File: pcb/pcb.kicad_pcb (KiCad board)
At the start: 2 copper layers, 35 x 88 mm, 41 parts, among them J1 NMJ4HCD2, J2 NMJ4HCD2, J3 694106301002, SW1 FSWITCH, U1 RC4558, U2 L78L09

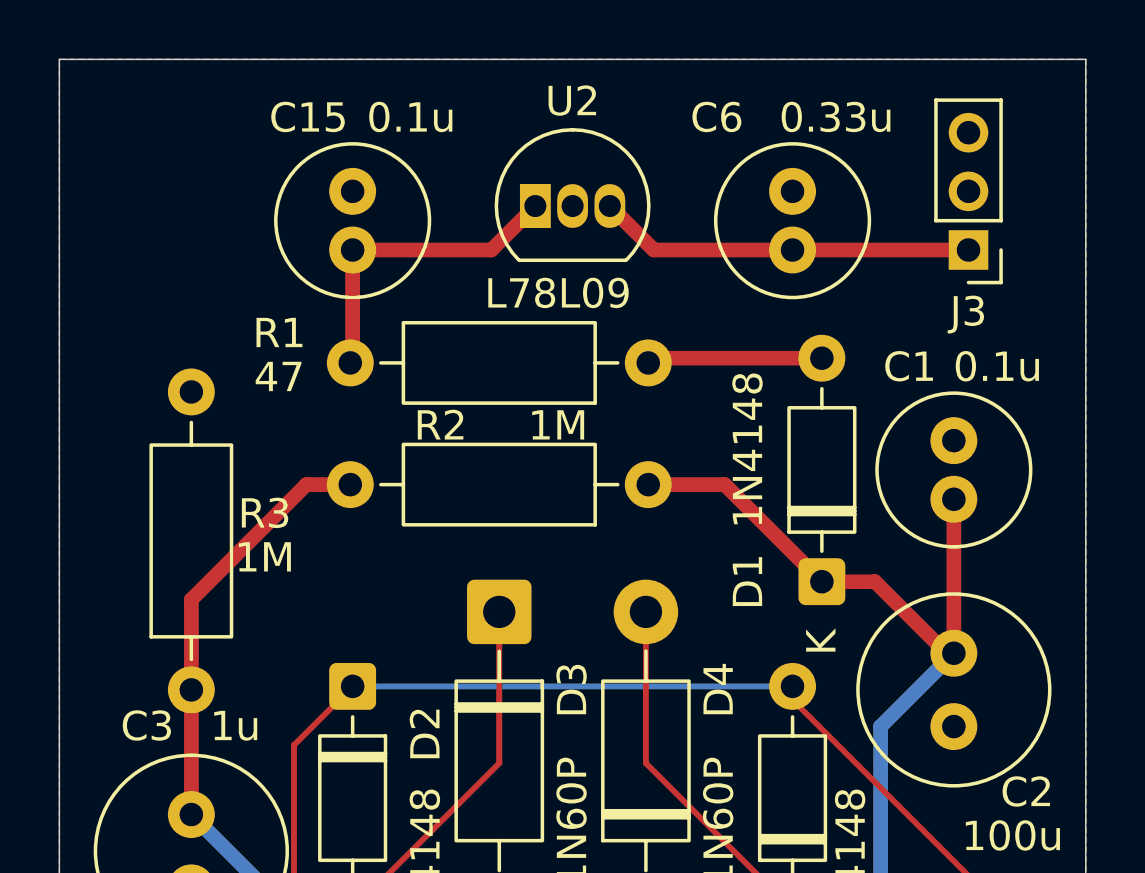
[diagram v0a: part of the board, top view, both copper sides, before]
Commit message: Fix reverse polarity protection diode - Move ahead of regulator
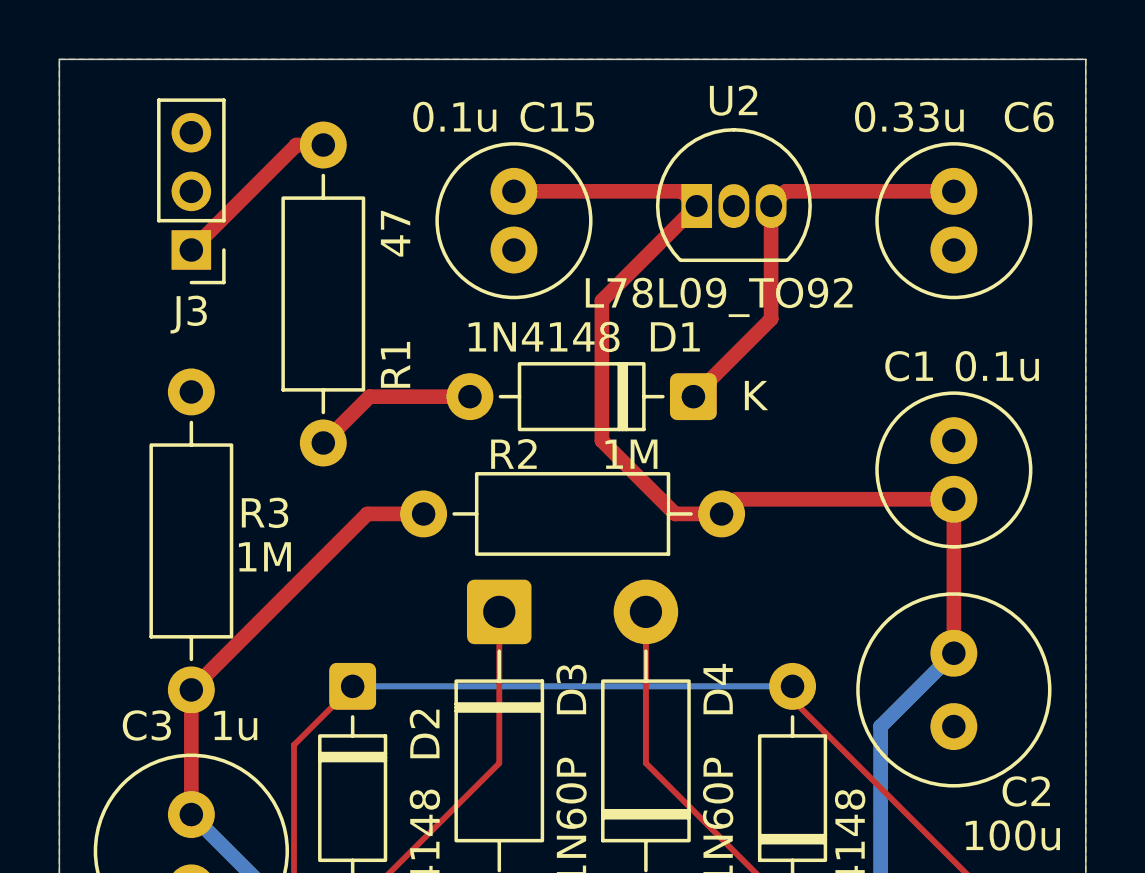
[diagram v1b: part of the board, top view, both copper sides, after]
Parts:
- U2: value L78L09 -> L78L09_TO92
- moved J3 26.5 mm to (162.0, 68.5)
- moved R1 11.4 mm to (166.5, 75.1), turned to 90 degrees
- moved D1 7.68 mm to (179.1, 73.5), turned to 180 degrees
- moved C15 5.85 mm to (173.0, 66.5), turned to -90 degrees
- moved C6 5.85 mm to (188.0, 66.5), turned to -90 degrees
- moved U2 5.50 mm to (179.2, 67.0)
- moved R2 2.69 mm to (180.1, 77.5)
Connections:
- C1 pad 1: /VCC -> /V9
- C14 pad 2: /VCC -> /V9
- C2 pad 1: /VCC -> /V9
- C6 pad 1: /VCCRAW -> Net-(D1-K)
- D1 pad 1: /VCC -> Net-(D1-K)
- R1 pad 2: /V9 -> /VCCRAW
- R2 pad 1: /VCC -> /V9
- SW1 pad 4: /VCC -> /V9
- U1 pad 8: /VCC -> /V9
- U2 pad 3: /VCCRAW -> Net-(D1-K)
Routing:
- net /V9: track 10.7 -> 97.1 mm
- net /VCC: track 80.9 -> 0.00 mm
- net Net-(D1-K): track 0.00 -> 14.0 mm
- net /VCCRAW: track 12.9 -> 5.98 mm
